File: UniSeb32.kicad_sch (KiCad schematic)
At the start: 61 parts, among them J1 IO, J101 Micro_SD_Card_Det, J2 ARJM11C7-114-BA-EW2, J3 Conn_02x05_Odd_Even, J6 SDS011, J7 Conn_01x02_Female, J8 Conn_01x02_Female, U1 mini_esp32, U2 LAN8720A, U3 AMS1117-3.3, U4 AMS5915, U5 module_bme280, U6 RT9400, U7 MCP23008-xSS, U8 HLK-PM01, X1 233-508, X2 233-503, X3 233-504

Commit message: .
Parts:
- removed JP3: SolderJumper_2_Open, Jumper:SolderJumper-2_P1.3mm_Open_Pad1.0x1.5mm, symbol Jumper:SolderJumper_2_Open
- added C5: 100n, Capacitor_SMD:C_0603_1608Metric, symbol Device:C_Small
- C14, C15: footprint Capacitor_SMD:C_0603_1608Metric -> Capacitor_SMD:C_1206_3216Metric
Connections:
- net 3V3-2: now also C5.2
- net GND: now also C5.1
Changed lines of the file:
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@@
   (junction (at 260.35 86.36) (diameter 0) (color 0 0 0 0)
   )
-  (junction (at 184.15 306.07) (diameter 0) (color 0 0 0 0)
-  )
   (junction (at 181.61 313.69) (diameter 0) (color 0 0 0 0)
   )
@@
   (junction (at 97.79 130.81) (diameter 0) (color 0 0 0 0)
   )
+  (junction (at 129.54 245.11) (diameter 0) (color 0 0 0 0)
+  )
   (junction (at 96.52 60.96) (diameter 0) (color 0 0 0 0)
   )
@@
   (junction (at 129.54 325.12) (diameter 0) (color 0 0 0 0)
   )
-  (junction (at 194.31 306.07) (diameter 0) (color 0 0 0 0)
-  )
   (junction (at 257.81 88.9) (diameter 0) (color 0 0 0 0)
   )
@@
     (stroke (width 0) (type default))
   )
-  (wire (pts (xy 138.43 281.94) (xy 158.75 281.94))
+  (wire (pts (xy 129.54 245.11) (xy 129.54 255.27))
     (stroke (width 0) (type default))
   )
-  (wire (pts (xy 194.31 306.07) (xy 193.04 306.07))
+  (wire (pts (xy 138.43 281.94) (xy 158.75 281.94))
     (stroke (width 0) (type default))
   )
@@
     (stroke (width 0) (type default))
   )
-  (wire (pts (xy 195.58 306.07) (xy 194.31 306.07))
-    (stroke (width 0) (type default))
-  )
   (wire (pts (xy 89.535 45.72) (xy 87.63 45.72))
     (stroke (width 0) (type default))
@@
     (stroke (width 0) (type default))
   )
-  (wire (pts (xy 184.15 304.165) (xy 194.31 304.165))
-    (stroke (width 0) (type default))
-  )
   (wire (pts (xy 257.81 88.9) (xy 257.81 102.235))
     (stroke (width 0) (type default))
@@
     (stroke (width 0) (type default))
   )
-  (wire (pts (xy 184.15 306.07) (xy 181.61 306.07))
+  (wire (pts (xy 181.61 306.07) (xy 195.58 306.07))
     (stroke (width 0) (type default))
   )
@@
     (stroke (width 0) (type default))
   )
-  (wire (pts (xy 129.54 230.505) (xy 129.54 255.27))
+  (wire (pts (xy 129.54 230.505) (xy 129.54 245.11))
     (stroke (width 0) (type default))
   )
@@
     (stroke (width 0) (type default))
   )
-  (wire (pts (xy 194.31 304.165) (xy 194.31 306.07))
-    (stroke (width 0) (type default))
-  )
   (polyline (pts (xy 20.32 22.86) (xy 20.32 111.76))
     (stroke (width 0) (type default))
@@
     (stroke (width 0) (type default))
   )
-  (wire (pts (xy 185.42 306.07) (xy 184.15 306.07))
-    (stroke (width 0) (type default))
-  )
   (wire (pts (xy 58.42 50.8) (xy 60.96 50.8))
     (stroke (width 0) (type default))
@@
     (stroke (width 0) (type default))
   )
-  (wire (pts (xy 184.15 306.07) (xy 184.15 304.165))
-    (stroke (width 0) (type default))
-  )
   (wire (pts (xy 129.54 325.12) (xy 129.54 323.85))
     (stroke (width 0) (type default))
@@
       (effects (font (size 1.27 1.27)) (justify left))
     )
-    (property "Footprint" "Capacitor_SMD:C_0603_1608Metric" (at 91.44 320.04 0)
+    (property "Footprint" "Capacitor_SMD:C_1206_3216Metric" (at 91.44 320.04 0)
       (effects (font (size 1.27 1.27)) hide)
     )
@@
     )
   )
+  (symbol (lib_id "power:GND") (at 124.46 245.11 270) (mirror x) (unit 1)
+    (in_bom yes) (on_board yes) (dnp no)
+    (property "Reference" "#PWR01" (at 118.11 245.11 0)
+      (effects (font (size 1.27 1.27)) hide)
+    )
+    (property "Value" "GND" (at 120.65 245.11 0)
+      (effects (font (size 1.27 1.27)))
+    )
+    (property "Footprint" "" (at 124.46 245.11 0)
+      (effects (font (size 1.27 1.27)) hide)
+    )
+    (property "Datasheet" "" (at 124.46 245.11 0)
+      (effects (font (size 1.27 1.27)) hide)
+    )
+    (pin "1")
+    (instances
+      (project "UniSeb32"
+        (path "/94c30dae-83f2-410e-815e-9e5d06243376"
+          (reference "#PWR01") (unit 1)
+        )
+      )
+    )
+  )
   (symbol (lib_id "Converter_ACDC:HLK-PM01") (at 71.12 76.2 0) (unit 1)
     (in_bom yes) (on_board yes) (dnp no) (fields_autoplaced)
@@
     )
   )
-  (symbol (lib_id "Jumper:SolderJumper_2_Open") (at 189.23 306.07 0) (unit 1)
-    (in_bom yes) (on_board yes) (dnp no)
-    (property "Reference" "JP3" (at 189.23 303.53 0)
-      (effects (font (size 1.27 1.27)))
-    )
-    (property "Value" "SolderJumper_2_Open" (at 189.23 304.0181 0)
-      (effects (font (size 1.27 1.27)) hide)
-    )
-    (property "Footprint" "Jumper:SolderJumper-2_P1.3mm_Open_Pad1.0x1.5mm" (at 189.23 306.07 0)
-      (effects (font (size 1.27 1.27)) hide)
-    )
-    (property "Datasheet" "~" (at 189.23 306.07 0)
-      (effects (font (size 1.27 1.27)) hide)
-    )
-    (pin "1")
-    (pin "2")
-    (instances
-      (project "UniSeb32"
-        (path "/94c30dae-83f2-410e-815e-9e5d06243376"
-          (reference "JP3") (unit 1)
-        )
-      )
-    )
-  )
   (symbol (lib_id "Connector:Micro_SD_Card_Det") (at 118.745 187.325 0) (unit 1)
     (in_bom yes) (on_board yes) (dnp no) (fields_autoplaced)
@@
     )
   )
+  (symbol (lib_id "Device:C_Small") (at 127 245.11 90) (unit 1)
+    (in_bom yes) (on_board yes) (dnp no)
+    (property "Reference" "C5" (at 128.27 249.555 0)
+      (effects (font (size 1.27 1.27)) (justify left))
+    )
+    (property "Value" "100n" (at 125.73 252.095 0)
+      (effects (font (size 1.27 1.27)) (justify left))
+    )
+    (property "Footprint" "Capacitor_SMD:C_0603_1608Metric" (at 127 245.11 0)
+      (effects (font (size 1.27 1.27)) hide)
+    )
+    (property "Datasheet" "~" (at 127 245.11 0)
+      (effects (font (size 1.27 1.27)) hide)
+    )
+    (property "LCSC" "C14663" (at 127 245.11 0)
+      (effects (font (size 1.27 1.27)) hide)
+    )
+    (property "JLC" "0603" (at 127 245.11 0)
+      (effects (font (size 1.27 1.27)) hide)
+    )
+    (pin "1")
+    (pin "2")
+    (instances
+      (project "UniSeb32"
+        (path "/94c30dae-83f2-410e-815e-9e5d06243376"
+          (reference "C5") (unit 1)
+        )
+      )
+    )
+  )
   (symbol (lib_id "Device:R") (at 152.4 300.99 0) (unit 1)
     (in_bom yes) (on_board yes) (dnp no)
-    (property "Reference" "R14" (at 156.21 299.72 0)
+    (property "Reference" "R14" (at 157.48 299.72 0)
       (effects (font (size 1.27 1.27)) (justify right))
     )
-    (property "Value" "12.1k" (at 158.75 302.26 0)
+    (property "Value" "12.1k" (at 159.385 302.26 0)
       (effects (font (size 1.27 1.27)) (justify right))
     )
@@
       (effects (font (size 1.27 1.27)) (justify left))
     )
-    (property "Footprint" "Capacitor_SMD:C_0603_1608Metric" (at 83.185 320.04 0)
+    (property "Footprint" "Capacitor_SMD:C_1206_3216Metric" (at 83.185 320.04 0)
       (effects (font (size 1.27 1.27)) hide)
     )

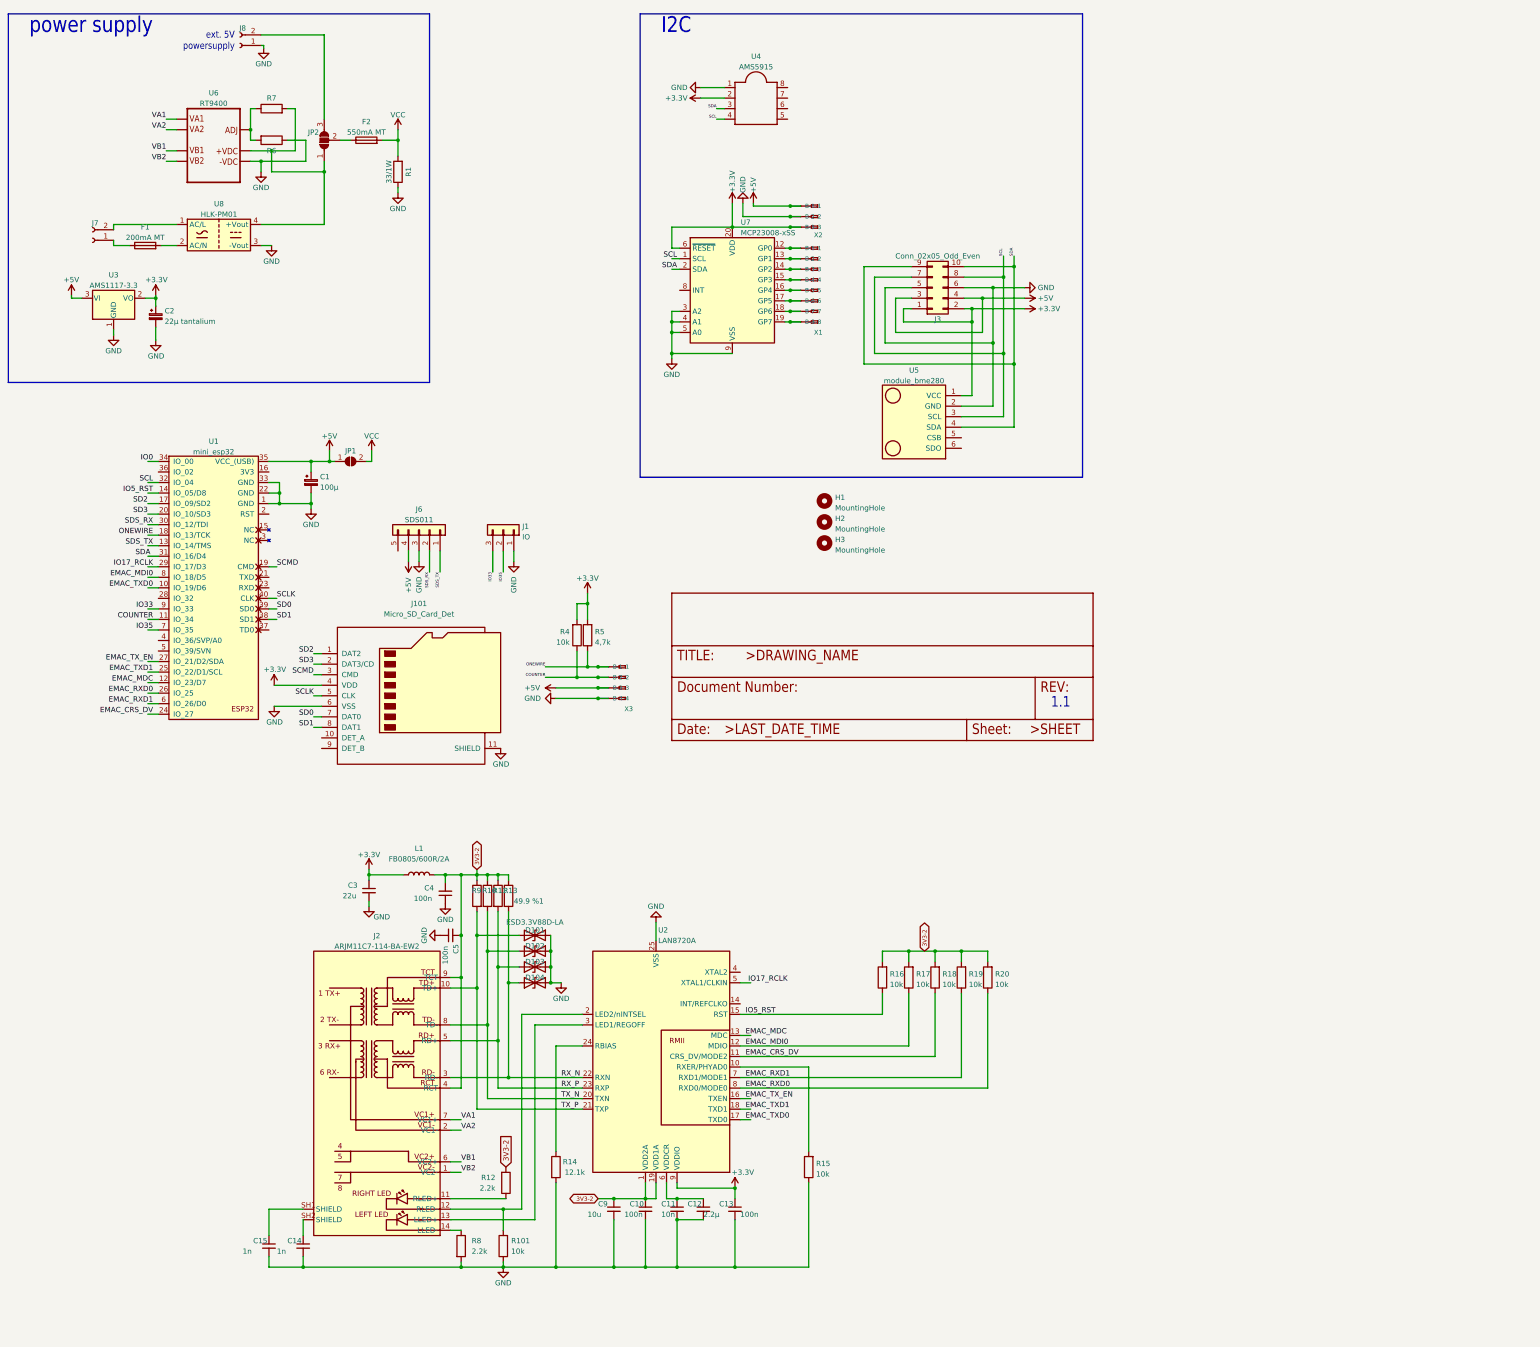
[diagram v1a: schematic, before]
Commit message: Changed PHY to RTL8201F
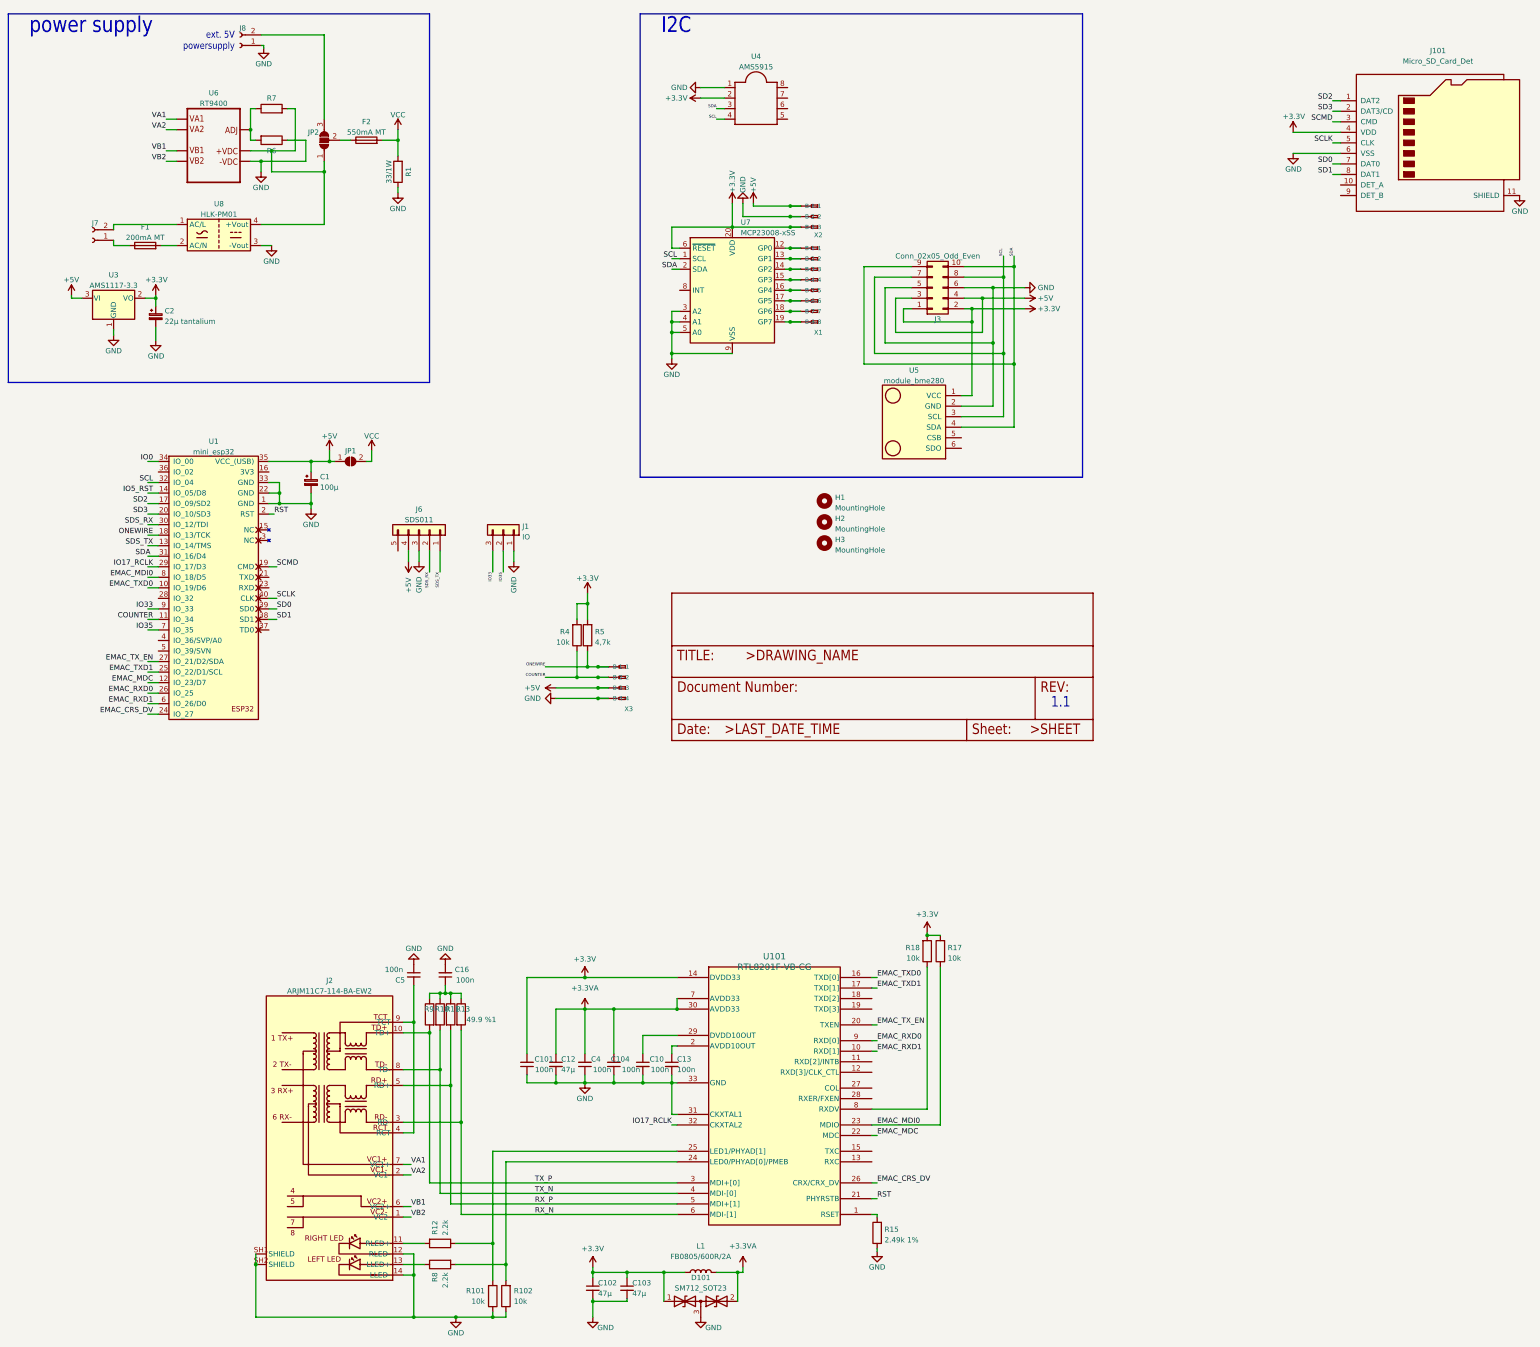
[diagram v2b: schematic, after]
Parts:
- removed C11: 10n, Capacitor_SMD:C_0603_1608Metric, symbol Device:C_Small
- removed C14, C15: 1n, Capacitor_SMD:C_1206_3216Metric, symbol Device:C_Small
- removed C3: 22u, Capacitor_SMD:C_1206_3216Metric, symbol Device:C_Small
- removed C9: 10u, Capacitor_SMD:C_0603_1608Metric, symbol Device:C_Small
- removed D101, D102, D103, D104: ESD3.3V88D-LA, Diode_SMD:D_SOD-923, symbol Diode:ESD9B3.3ST5G
- removed R14: 12.1k, Resistor_SMD:R_0603_1608Metric, symbol Device:R
- removed R16, R19, R20: 10k, Resistor_SMD:R_0603_1608Metric, symbol Device:R
- removed U2: LAN8720A, Package_DFN_QFN:QFN-24-1EP_4x4mm_P0.5mm_EP2.6x2.6mm, symbol Interface_Ethernet:LAN8720A
- added C101, C104, C16: 100n, Capacitor_SMD:C_0603_1608Metric, symbol Device:C_Small
- added C102, C103: 47µ, Capacitor_SMD:C_0805_2012Metric, symbol Device:C_Small
- added D101: SM712_SOT23, Package_TO_SOT_SMD:SOT-23, symbol Diode:SM712_SOT23
- added R102: 10k, Resistor_SMD:R_0603_1608Metric, symbol Device:R
- added U101: RTL8201F-VB-CG, UniSeb32:QFN_8201F-VB-CG_RTK, symbol RTL8201F:RTL8201F-VB-CG
- C12: value 2.2µ -> 47µ; footprint Capacitor_SMD:C_0603_1608Metric -> Capacitor_SMD:C_0805_2012Metric; LCSC C23630 -> C2844386
- R15: value 10k -> 2.49k 1%; LCSC C25804 -> C203449
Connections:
- net +3.3V: now also R17.2, R18.2, C101.2, C102.1, C103.1, D101.1 (A1), U101.14 (DVDD33); no longer C13.1
- net EMAC_CRS_DV: now also U101.26 (CRX/CRX_DV); no longer R18.1
- net EMAC_MDC: now also U101.22 (MDC)
- net EMAC_MDI0: now also U101.23 (MDIO)
- net EMAC_RXD0: now also U101.9 (RXD[0])
- net EMAC_RXD1: now also U101.10 (RXD[1])
- net EMAC_TXD0: now also U101.16 (TXD[0])
- net EMAC_TXD1: now also U101.17 (TXD[1])
- net EMAC_TX_EN: now also U101.20 (TXEN)
- net GND: now also J2.12 (RLED-), J2.14 (LLED-), J2.SH1 (SHIELD), J2.SH2 (SHIELD), C101.1, C102.2, C103.2, C104.1, C16.2, D101.3 (common), R102.1, U101.31 (CKXTAL1), U101.33 (GND); no longer R8.2
- net IO17_RCLK: now also U101.32 (CKXTAL2)
- net RX_N: now also U101.6 (MDI-[1])
- net RX_P: now also U101.5 (MDI+[1])
- net TX_N: now also U101.4 (MDI-[0])
- net TX_P: now also U101.3 (MDI+[0])
- net at R12.1: now also R101.2, U101.25 (LED1/PHYAD[1]); no longer J2.11 (RLED+)
- net at R15.2: now also U101.1 (RSET)
- net at J2.13 (LLED+): now also R8.1
- net +3.3VA: now reaches C12.1
- net +3.3VA: now also C4.2, L1.2, C104.2, D101.2 (A2), U101.30 (AVDD33), U101.7 (AVDD33)
- net RST: now reaches U1.2 (RST)
- net RST: now also U101.21 (PHYRSTB)
- removed net 3V3-2: C10.1, C4.2, C5.2, J2.4 (RCT), J2.9 (TCT), L1.2, R10.1, R11.1, R12.2, R13.1, R17.2, R18.2, R9.1
- new net: C10.1, U101.29 (DVDD10OUT)
- new net: J2.11 (RLED+), R12.2
- new net: C16.1, R10.1, R11.1, R13.1, R9.1
- new net: C5.2, J2.4 (RCT), J2.9 (TCT)
- new net: C13.1, U101.2 (AVDD10OUT)
- new net: R102.2, R8.2, U101.24 (LED0/PHYAD[0]/PMEB)
- new net: R18.1, U101.8 (RXDV)
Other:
- moved on the sheet: C10, C12, C13, C4, C5, J101, J2, L1, R10, R101, R11, R12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
